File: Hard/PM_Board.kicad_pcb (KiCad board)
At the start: 2 copper layers, 70 x 70 mm, 84 parts, among them J1 Micro_SD_Card_Det_Hirose_DM3AT, J101 LiPo_V+, J102 LiPo_V-, J2 KRC_Conn_SWD, J3 USB_B_Micro, J4 KRC_Conn_CAN, J5 KRC_Conn_CAN, J6 Umbilical, Q1 SSM6J501NU, Q2 2n7002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

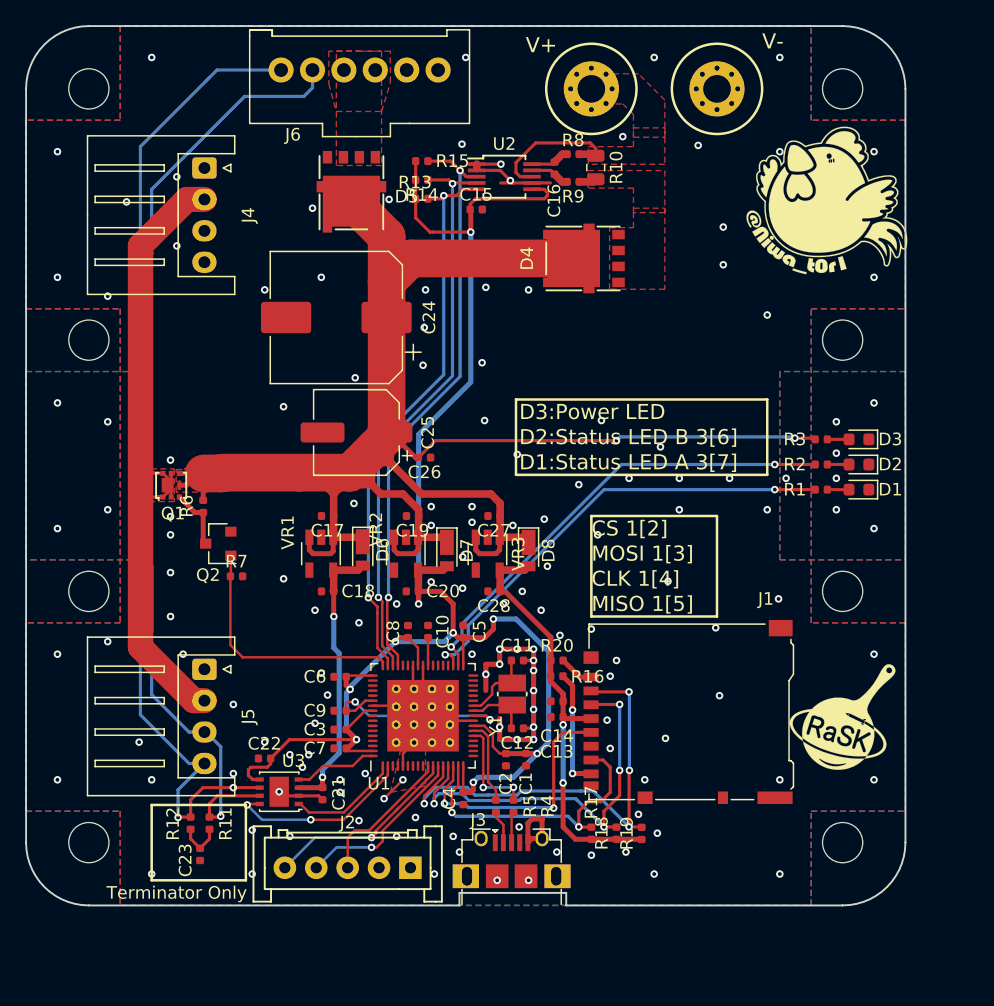
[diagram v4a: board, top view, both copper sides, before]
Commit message: [add] ダイオードの選定を変更。PchMOSFETの選定を変更。パターンを引き直し。ガーバ出力
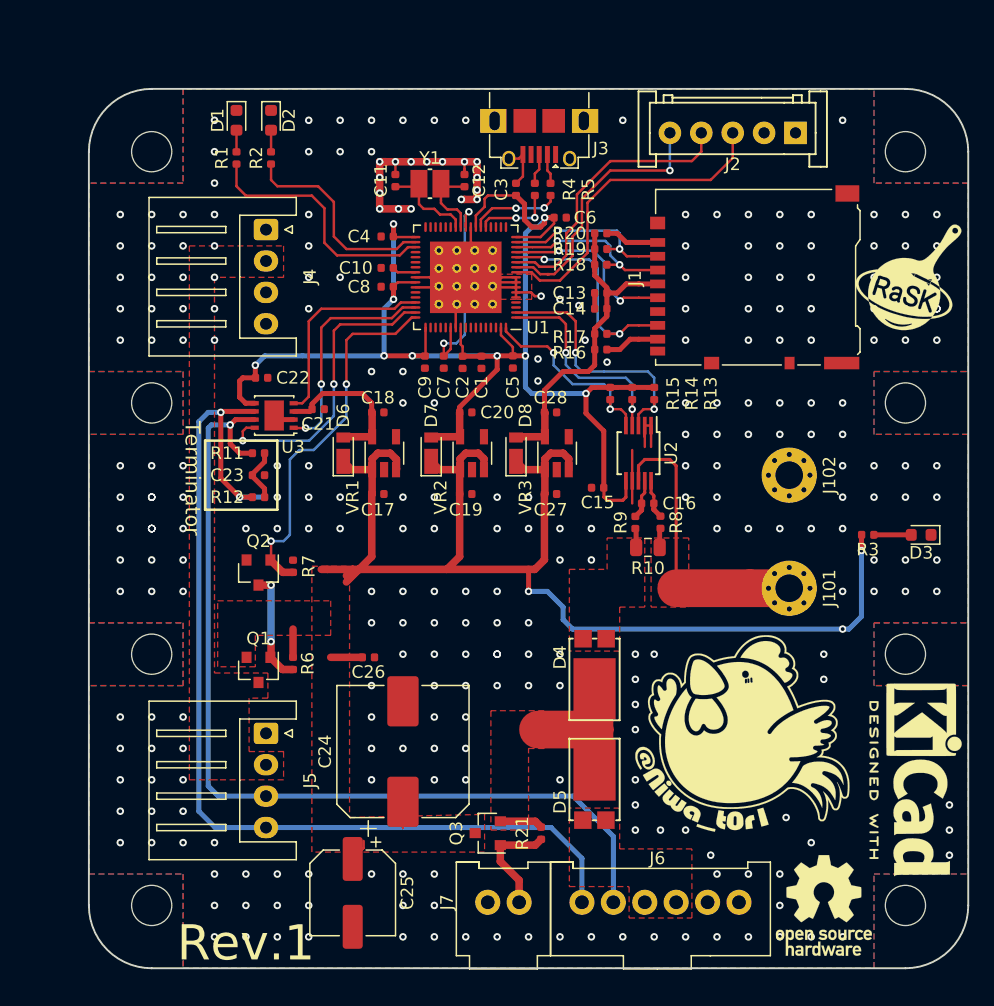
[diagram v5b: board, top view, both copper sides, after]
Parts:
- removed the G*** at (176.2, 83.8)
- removed the REF** at (177.5, 95.0)
- removed the REF** at (117.5, 115.0)
- removed the REF** at (117.5, 95.0)
- removed the REF** at (177.5, 75.0)
- removed the REF** at (177.5, 135.0)
- removed the REF** at (117.5, 135.0)
- removed the REF** at (117.5, 75.0)
- removed the REF** at (177.5, 115.0)
- added G***: LOGO, logo:niwa, F.Cu at (169.5, 126.2)
- added J7: SW, KUTKiCad_footprint:Hirose_DF1E_DF1E-2P-2.5DS_1x02_P2.5mm_Vertical, F.Cu at (151.8, 139.8)
- added Q3: SSM3J328R, Package_TO_SOT_SMD:SOT-23, F.Cu at (149.2, 134.2)
- added R21: 10k, Resistor_SMD:R_0402_1005Metric, F.Cu at (153.5, 134.2)
- added REF**: MountingHole_3.2mm_M3, MountingHole:MountingHole_3.2mm_M3, F.Cu at (122.5, 120.0)
- added REF**: OSHW-Logo_7.5x8mm_SilkScreen, Symbol:OSHW-Logo_7.5x8mm_SilkScreen, F.Cu at (176.0, 140.0)
- added REF**: MountingHole_3.2mm_M3, MountingHole:MountingHole_3.2mm_M3, F.Cu at (182.5, 120.0)
- added REF**: MountingHole_3.2mm_M3, MountingHole:MountingHole_3.2mm_M3, F.Cu at (182.5, 100.0)
- added REF**: MountingHole_3.2mm_M3, MountingHole:MountingHole_3.2mm_M3, F.Cu at (122.5, 100.0)
- added REF**: MountingHole_3.2mm_M3, MountingHole:MountingHole_3.2mm_M3, F.Cu at (122.5, 140.0)
- added REF**: MountingHole_3.2mm_M3, MountingHole:MountingHole_3.2mm_M3, F.Cu at (182.5, 140.0)
- added REF**: MountingHole_3.2mm_M3, MountingHole:MountingHole_3.2mm_M3, F.Cu at (182.5, 80.0)
- added REF**: MountingHole_3.2mm_M3, MountingHole:MountingHole_3.2mm_M3, F.Cu at (122.5, 80.0)
- added REF**: KiCad-Logo2_6mm_SilkScreen, Symbol:KiCad-Logo2_6mm_SilkScreen, F.Cu at (184.0, 130.0)
- D4, D5: value NTS1545 -> SDM8M100P5; footprint KUTKiCad_footprint:DFN5_5x6_1.27P -> KUTKiCad_footprint:D_PowerDI5
- Q1: value SSM6J501NU -> SSM3J328R; footprint KUTKiCad_footprint:UDFN6B -> Package_TO_SOT_SMD:SOT-23
- R6, R7: value 1k -> 10k
- moved J6 70.4 mm to (169.2, 139.8)
- moved J2 66.0 mm to (173.8, 78.5)
- moved J3 60.2 mm to (153.3, 77.5), turned to 180 degrees
- moved D1 57.6 mm to (129.2, 77.5), turned to 270 degrees
- moved D2 54.2 mm to (132.0, 77.5), turned to 270 degrees
- moved R1 53.5 mm to (129.2, 80.5), turned to 90 degrees
- moved D5 51.6 mm to (157.8, 131.8)
- moved G*** 50.7 mm to (164.8, 131.0)
- moved R2 50.1 mm to (132.0, 80.5), turned to 90 degrees
- moved R5 49.3 mm to (154.2, 83.0), turned to 270 degrees
- moved R4 49.1 mm to (153.0, 83.0), turned to 270 degrees
- moved R19 46.6 mm to (158.2, 87.8), turned to 0 degrees
- moved R18 45.3 mm to (158.2, 89.0), turned to 0 degrees
- moved C3 45.2 mm to (151.5, 83.0), turned to 90 degrees
- moved C4 45.1 mm to (141.2, 86.8), turned to 180 degrees
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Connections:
- C17 pad 1: VCC -> Net-(C17-Pad1)
- C19 pad 1: VCC -> Net-(C17-Pad1)
- C24 pad 1: VCC -> Net-(C17-Pad1)
- C25 pad 1: VCC -> Net-(C17-Pad1)
- C26 pad 2: VCC -> Net-(C17-Pad1)
- C27 pad 1: VCC -> Net-(C17-Pad1)
- D6 pad 1: VCC -> Net-(C17-Pad1)
- D7 pad 1: VCC -> Net-(C17-Pad1)
- D8 pad 1: VCC -> Net-(C17-Pad1)
- Q1 pad 1: Net-(J4-Pad2) -> Net-(Q1-Pad1)
- Q1 pad 2: Net-(J4-Pad2) -> Net-(C17-Pad1)
- Q1 pad 3: Net-(Q1-Pad3) -> Net-(J4-Pad2)
- Q2 pad 3: Net-(Q1-Pad3) -> Net-(Q1-Pad1)
- R13 pad 2: /INA226_SCL -> /INA226_Alert
- R15 pad 2: /INA226_Alert -> /INA226_SCL
- R3 pad 2: VCC -> Net-(C17-Pad1)
- R6 pad 1: VCC -> Net-(C17-Pad1)
- R6 pad 2: Net-(Q1-Pad3) -> Net-(Q1-Pad1)
- U1 pad 1: /CAN_TXD -> /INA226_SDA
- U1 pad 13: /SD_CS -> /SD_MISO
- U1 pad 14: /SD_MOSI -> /SD_CLK
- U1 pad 15: /SD_CLK -> /SD_MOSI
- U1 pad 16: /SD_MISO -> /SD_CS
- U1 pad 2: /CAN_STB -> /INA226_Alert
- U1 pad 48: /INA226_Alert -> /CAN_RXD
- U1 pad 49: /INA226_SDA -> /CAN_TXD
- U1 pad 50: /INA226_SCL -> /CAN_STB
- U1 pad 68: /CAN_RXD -> /INA226_SCL
- VR1 pad 1: VCC -> Net-(C17-Pad1)
- VR1 pad 3: VCC -> Net-(C17-Pad1)
- VR2 pad 1: VCC -> Net-(C17-Pad1)
- VR2 pad 3: VCC -> Net-(C17-Pad1)
- VR3 pad 1: VCC -> Net-(C17-Pad1)
- VR3 pad 3: VCC -> Net-(C17-Pad1)
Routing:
- net VCC: track 182.9 -> 14.4 mm, vias 2 -> 0
- net Net-(C17-Pad1): track 0.00 -> 109.5 mm, vias 0 -> 3
- net Net-(J4-Pad2): track 55.5 -> 0.00 mm
- net /INA226_SCL: track 44.7 -> 15.7 mm
- net /INA226_SDA: track 45.3 -> 17.4 mm
- net /INA226_Alert: track 46.6 -> 20.8 mm
- net /SD_CS: track 37.1 -> 14.2 mm, vias 4 -> 2
- net +3V3: track 138.9 -> 116.1 mm
- net Net-(R2-Pad1): track 37.3 -> 16.9 mm, vias 2 -> 0
- net /SD_MOSI: track 32.4 -> 13.9 mm, vias 4 -> 2
- net Net-(R1-Pad1): track 37.0 -> 20.2 mm, vias 2 -> 0
- net Net-(J2-Pad3): track 11.4 -> 26.1 mm
- net +BATT: track 11.3 -> 24.9 mm
- net +5V: track 22.3 -> 12.4 mm, vias 2 -> 0
- net /CAN_RXD: track 6.68 -> 16.5 mm
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- added copper zone on F.Cu, net Net-(C17-Pad1)
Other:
- outline, holes or cut-outs redrawn
- board text added: "GS-8 Power Management Board Rev.1 Designed by T.Niwa 2019.9"
- board text added: "Rev.1"
- board text added: "Terminator"
- board text removed: "CAN-H"
- board text removed: "CAN-L"
- board text removed: "CLK"
- board text removed: "CLK 1[4]"
- board text removed: "CS 1[2]"
- board text removed: "D1:Status LED A 3[7]"
- board text removed: "D2:Status LED B 3[6]"
- board text removed: "D3:Power LED"
- board text removed: "DIO"
- board text removed: "Date"
- board text removed: "GND"
- board text removed: "GS-8 PM Board Rev.1 Designed by T.Niwa 2019.9"
- board text removed: "MISO 1[5]"
- board text removed: "MOSI 1[3]"
- board text removed: "Manufacturer"
- board text removed: "NC"
- board text removed: "Note"
- board text removed: "RES"
- board text removed: "Terminator Only"
- board text removed: "V+"
- board text removed: "V-"
- board text removed: "VCC"

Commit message: [update] パスコンの位置を変更
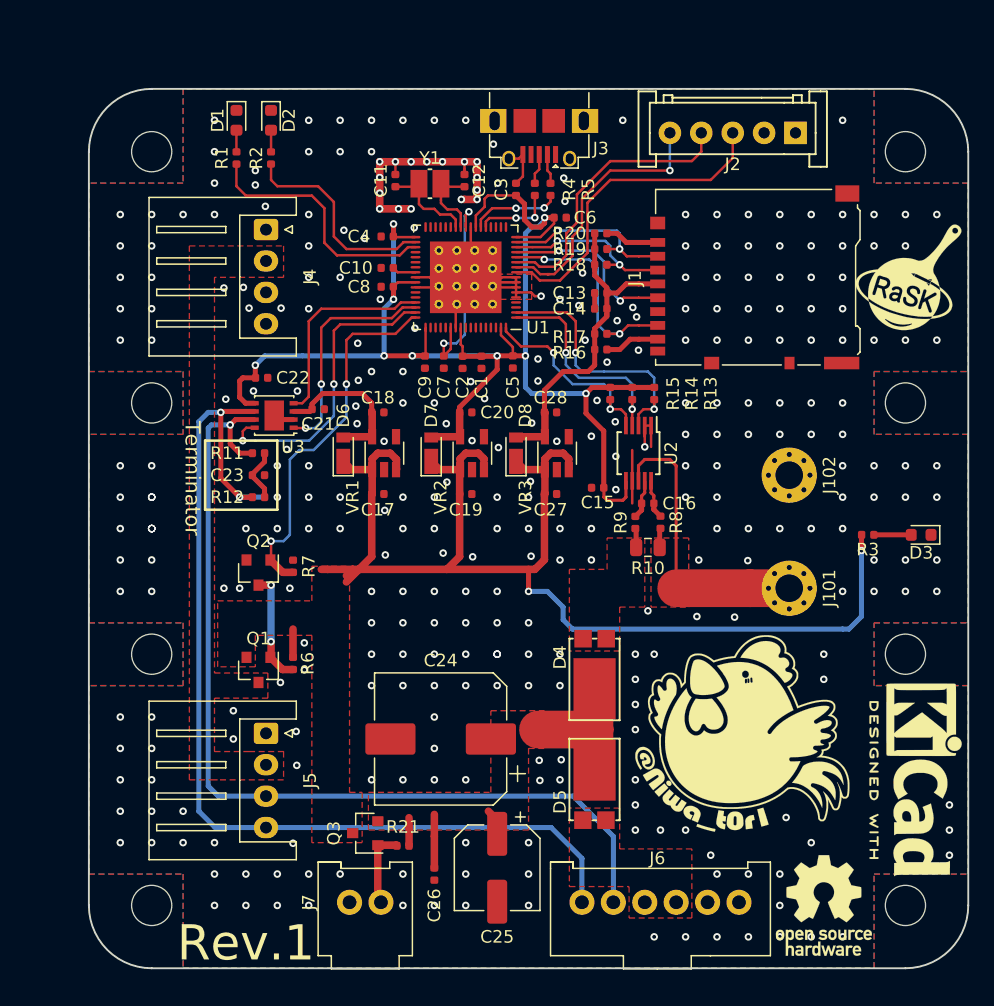
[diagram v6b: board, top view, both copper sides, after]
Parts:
- moved C26 18.0 mm to (145.0, 137.5), turned to 90 degrees
- moved C25 11.7 mm to (150.0, 137.0)
- moved R21 11.0 mm to (142.5, 135.2), turned to 180 degrees
- moved J7 11.0 mm to (140.8, 139.8)
- moved Q3 9.75 mm to (139.5, 134.2)
- moved C24 3.16 mm to (145.5, 126.8), turned to 180 degrees
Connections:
- C24 pad 1: Net-(C17-Pad1) -> VCC
- C25 pad 1: Net-(C17-Pad1) -> VCC
- C26 pad 2: Net-(C17-Pad1) -> VCC
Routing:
- net Net-(C17-Pad1): track 109.5 -> 103.1 mm, vias 3 -> 2
- net VCC: track 14.4 -> 20.3 mm
- net Net-(J7-Pad1): track 8.61 -> 6.19 mm
- net GND: vias 292 -> 336
